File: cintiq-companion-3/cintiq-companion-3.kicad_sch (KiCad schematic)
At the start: 4 parts, among them J1 13HD_eDP, J2 13HD_penpanel, J3 13HD_buttonboard, J4 13HD_fingerpanel

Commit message: rotated images + ran some signals
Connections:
- net at J2.13 (Pin_13): now also J3.10 (Pin_10)
- net at J2.17 (Pin_17): now also J3.11 (Pin_11)
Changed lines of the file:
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@@
+	(wire
+		(pts
+			(xy 170.18 31.75) (xy 170.18 46.99)
+		)
+		(stroke
+			(width 0)
+			(type default)
+		)
+	)
 	(wire
 		(pts
@@
 	(wire
 		(pts
+			(xy 73.66 31.75) (xy 73.66 49.53)
+		)
+		(stroke
+			(width 0)
+			(type default)
+		)
+	)
+	(wire
+		(pts
 			(xy 157.48 33.02) (xy 151.13 33.02)
 		)
@@
 	(wire
 		(pts
+			(xy 170.18 46.99) (xy 83.82 46.99)
+		)
+		(stroke
+			(width 0)
+			(type default)
+		)
+	)
+	(wire
+		(pts
 			(xy 88.9 33.02) (xy 104.14 33.02)
 		)
@@
 	(wire
 		(pts
+			(xy 73.66 49.53) (xy 172.72 49.53)
+		)
+		(stroke
+			(width 0)
+			(type default)
+		)
+	)
+	(wire
+		(pts
 			(xy 248.92 64.77) (xy 248.92 109.22)
 		)
@@
 	(wire
 		(pts
+			(xy 83.82 46.99) (xy 83.82 31.75)
+		)
+		(stroke
+			(width 0)
+			(type default)
+		)
+	)
+	(wire
+		(pts
 			(xy 48.26 93.98) (xy 48.26 80.01)
 		)
 		(stroke
+			(width 0)
+			(type default)
+		)
+	)
+	(wire
+		(pts
+			(xy 172.72 31.75) (xy 172.72 49.53)
+		)
+		(stroke

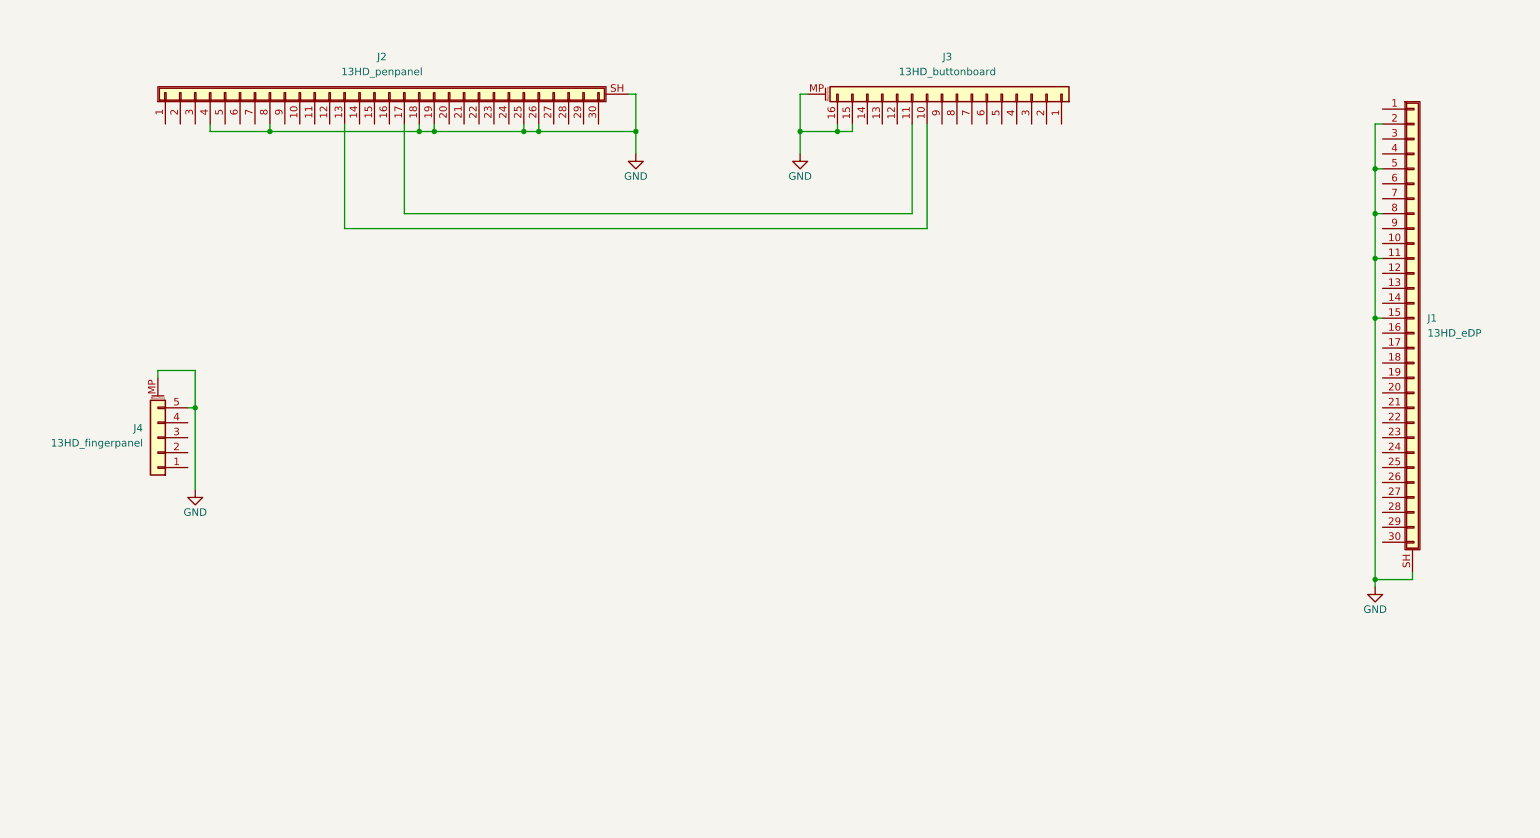
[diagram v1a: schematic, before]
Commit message: Added CP2102 usb uart bridge
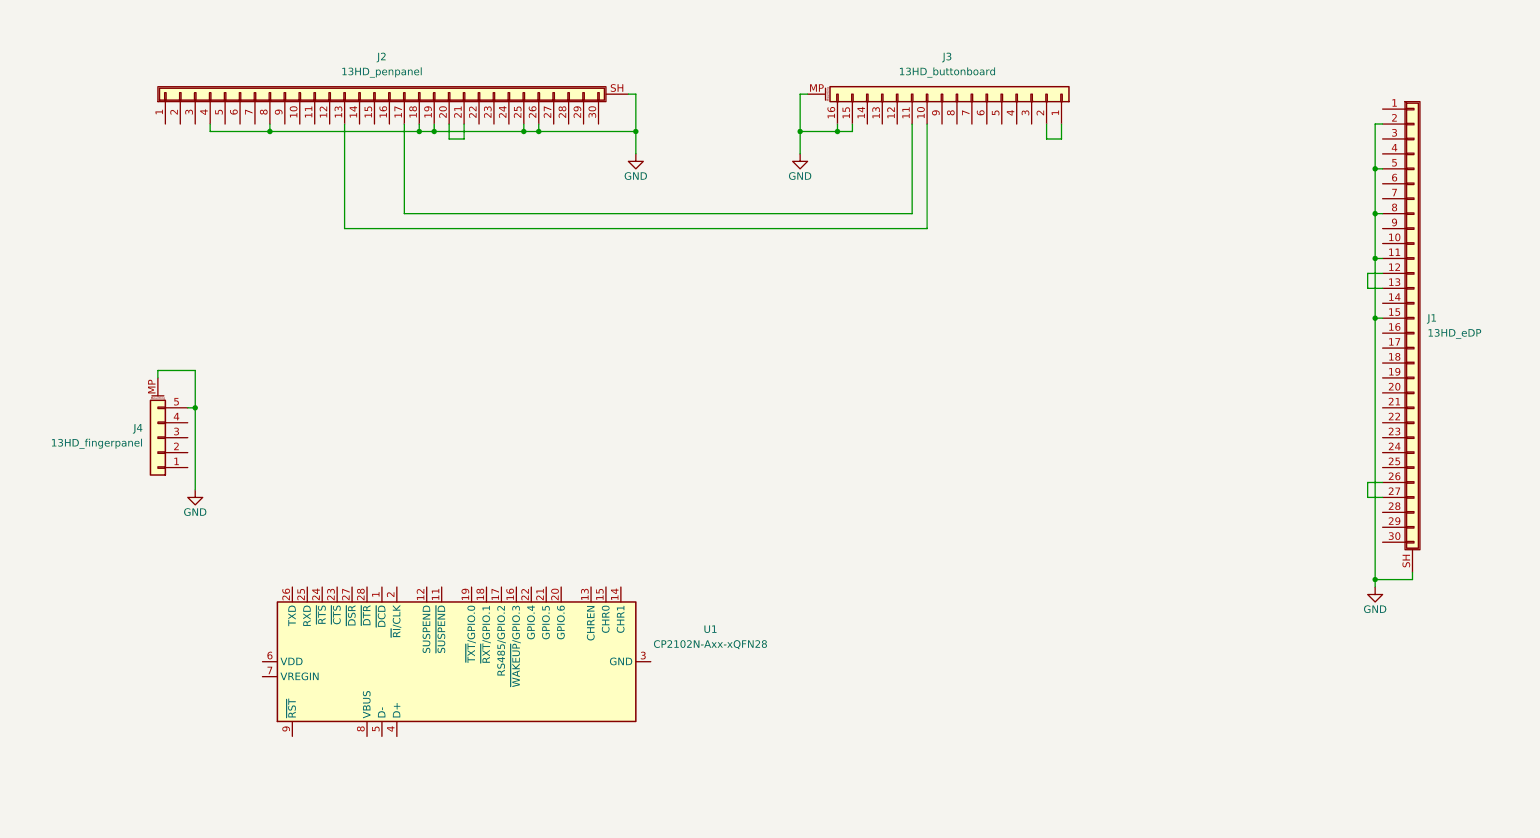
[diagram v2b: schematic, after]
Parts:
- added U1: CP2102N-Axx-xQFN28, Package_DFN_QFN:QFN-28-1EP_5x5mm_P0.5mm_EP3.35x3.35mm, symbol Interface_USB:CP2102N-Axx-xQFN28
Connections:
- net at J2.20 (Pin_20): now also J2.21 (Pin_21)
- net at J3.1 (Pin_1): now also J3.2 (Pin_2)
- net at J1.12 (Pin_12): now also J1.13 (Pin_13)
- net at J1.26 (Pin_26): now also J1.27 (Pin_27)
- new net: U1.29 (GND), U1.3 (GND)
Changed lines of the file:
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@@
+	(wire
+		(pts
+			(xy 195.58 34.29) (xy 193.04 34.29)
+		)
+		(stroke
+			(width 0)
+			(type default)
+		)
+	)
 	(wire
 		(pts
@@
 	(wire
 		(pts
+			(xy 250.19 57.15) (xy 247.65 57.15)
+		)
+		(stroke
+			(width 0)
+			(type default)
+		)
+	)
+	(wire
+		(pts
+			(xy 247.65 92.71) (xy 250.19 92.71)
+		)
+		(stroke
+			(width 0)
+			(type default)
+		)
+	)
+	(wire
+		(pts
 			(xy 170.18 31.75) (xy 170.18 46.99)
 		)
@@
 	(wire
 		(pts
+			(xy 250.19 95.25) (xy 247.65 95.25)
+		)
+		(stroke
+			(width 0)
+			(type default)
+		)
+	)
+	(wire
+		(pts
 			(xy 104.14 31.75) (xy 104.14 33.02)
 		)
@@
 	(wire
 		(pts
+			(xy 93.98 31.75) (xy 93.98 34.29)
+		)
+		(stroke
+			(width 0)
+			(type default)
+		)
+	)
+	(wire
+		(pts
+			(xy 247.65 59.69) (xy 250.19 59.69)
+		)
+		(stroke
+			(width 0)
+			(type default)
+		)
+	)
+	(wire
+		(pts
 			(xy 151.13 36.83) (xy 151.13 33.02)
 		)
@@
 	(wire
 		(pts
+			(xy 247.65 95.25) (xy 247.65 92.71)
+		)
+		(stroke
+			(width 0)
+			(type default)
+		)
+	)
+	(wire
+		(pts
 			(xy 106.68 33.02) (xy 123.19 33.02)
 		)
@@
 	(wire
 		(pts
+			(xy 91.44 34.29) (xy 91.44 31.75)
+		)
+		(stroke
+			(width 0)
+			(type default)
+		)
+	)
+	(wire
+		(pts
+			(xy 195.58 31.75) (xy 195.58 34.29)
+		)
+		(stroke
+			(width 0)
+			(type default)
+		)
+	)
+	(wire
+		(pts
 			(xy 248.92 64.77) (xy 248.92 109.22)
 		)
@@
 	(wire
 		(pts
+			(xy 193.04 34.29) (xy 193.04 31.75)
+		)
+		(stroke
+			(width 0)
+			(type default)
+		)
+	)
+	(wire
+		(pts
 			(xy 60.96 33.02) (xy 86.36 33.02)
 		)
@@
 	(wire
 		(pts
+			(xy 247.65 57.15) (xy 247.65 59.69)
+		)
+		(stroke
+			(width 0)
+			(type default)
+		)
+	)
+	(wire
+		(pts
 			(xy 123.19 33.02) (xy 123.19 26.67)
+		)
+		(stroke
+			(width 0)
+			(type default)
+		)
+	)
+	(wire
+		(pts
+			(xy 93.98 34.29) (xy 91.44 34.29)
 		)
 		(stroke
@@
 					(unit 1)
 				)
+			)
+		)
+	)
+	(symbol
+		(lib_id "Interface_USB:CP2102N-Axx-xQFN28")
+		(at 92.71 123.19 90)
+		(unit 1)
+		(exclude_from_sim no)
+		(in_bom yes)
+		(on_board yes)
+		(dnp no)
+		(fields_autoplaced yes)
+		(property "Reference" "U1"
+			(at 135.89 117.6938 90)
+			(effects
+				(font
+					(size 1.27 1.27)
+				)
+			)
+		)
+		(property "Value" "CP2102N-Axx-xQFN28"
+			(at 135.89 120.2338 90)
+			(effects
+				(font
+					(size 1.27 1.27)
+				)
+			)
+		)
+		(property "Footprint" "Package_DFN_QFN:QFN-28-1EP_5x5mm_P0.5mm_EP3.35x3.35mm"
+			(at 124.46 90.17 0)
+			(effects
+				(font
+					(size 1.27 1.27)
+				)
+				(hide yes)
+			)
+		)
+		(property "Datasheet" "https://www.silabs.com/documents/public/data-sheets/cp2102n-datasheet.pdf"
+			(at 111.76 121.92 0)
+			(effects
+				(font
+					(size 1.27 1.27)
+				)
+				(hide yes)
+			)
+		)
+		(property "Description" "USB to UART master bridge, QFN-28"
+			(at 92.71 123.19 0)
+			(effects
+				(font
+					(size 1.27 1.27)
+				)
+				(hide yes)
+			)
+		)
+		(pin "13"
+		)
+		(pin "5"
+		)
+		(pin "29"
+		)
+		(pin "2"
+		)
+		(pin "9"
+		)
+		(pin "23"
+		)
+		(pin "24"
+		)
+		(pin "25"
+		)
+		(pin "15"
+		)
+		(pin "26"
+		)
+		(pin "3"
+		)
+		(pin "7"
+		)
+		(pin "8"
+		)
+		(pin "14"
+		)
+		(pin "1"
+		)
+		(pin "18"
+		)
+		(pin "19"
+		)
+		(pin "17"
+		)
+		(pin "21"
+		)
+		(pin "22"
+		)
+		(pin "27"
+		)
+		(pin "11"
+		)
+		(pin "12"
+		)
+		(pin "10"
+		)
+		(pin "16"
+		)
+		(pin "20"
+		)
+		(pin "28"
+		)
+		(pin "4"
+		)
+		(pin "6"
+		)
+		(instances
+			(project "cintiq-companion-3"
+				(path "/ef92970f-f7a1-4011-9c13-6d46a45b923d"
+					(reference "U1")
+					(unit 1)
+				)

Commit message: Added USB pins for touch and pen panels
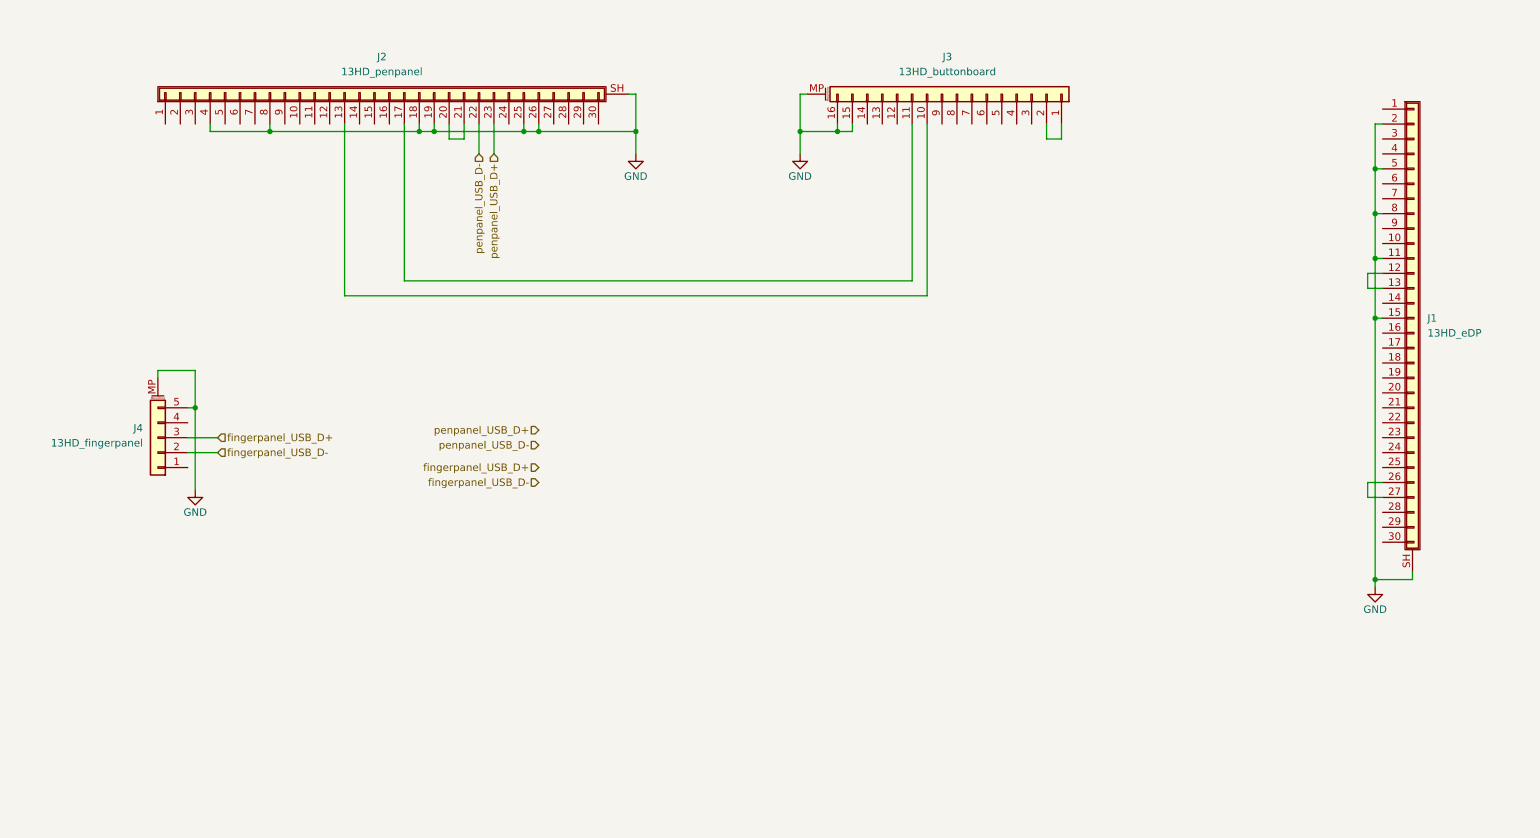
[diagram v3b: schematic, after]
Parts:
- removed U1: CP2102N-Axx-xQFN28, Package_DFN_QFN:QFN-28-1EP_5x5mm_P0.5mm_EP3.35x3.35mm, symbol Interface_USB:CP2102N-Axx-xQFN28
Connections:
- net penpanel_USB_D-: now reaches J2.22 (Pin_22)
- net penpanel_USB_D+: now reaches J2.23 (Pin_23)
- net fingerpanel_USB_D-: now reaches J4.2 (Pin_2)
- net fingerpanel_USB_D+: now reaches J4.3 (Pin_3)
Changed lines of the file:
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@@
 	(wire
 		(pts
-			(xy 170.18 31.75) (xy 170.18 46.99)
+			(xy 170.18 31.75) (xy 170.18 58.42)
 		)
 		(stroke
@@
 	(wire
 		(pts
+			(xy 52.07 85.09) (xy 46.99 85.09)
+		)
+		(stroke
+			(width 0)
+			(type default)
+		)
+	)
+	(wire
+		(pts
 			(xy 250.19 31.75) (xy 248.92 31.75)
 		)
@@
 	(wire
 		(pts
-			(xy 73.66 31.75) (xy 73.66 49.53)
+			(xy 73.66 31.75) (xy 73.66 60.96)
 		)
 		(stroke
@@
 	(wire
 		(pts
-			(xy 170.18 46.99) (xy 83.82 46.99)
+			(xy 170.18 58.42) (xy 83.82 58.42)
 		)
 		(stroke
@@
 	(wire
 		(pts
-			(xy 73.66 49.53) (xy 172.72 49.53)
+			(xy 73.66 60.96) (xy 172.72 60.96)
 		)
 		(stroke
@@
 	(wire
 		(pts
-			(xy 83.82 46.99) (xy 83.82 31.75)
+			(xy 83.82 58.42) (xy 83.82 31.75)
 		)
 		(stroke
@@
 	(wire
 		(pts
-			(xy 172.72 31.75) (xy 172.72 49.53)
+			(xy 172.72 31.75) (xy 172.72 60.96)
 		)
 		(stroke
@@
 	(wire
 		(pts
+			(xy 99.06 36.83) (xy 99.06 31.75)
+		)
+		(stroke
+			(width 0)
+			(type default)
+		)
+	)
+	(wire
+		(pts
 			(xy 160.02 33.02) (xy 157.48 33.02)
 		)
@@
 	(wire
 		(pts
+			(xy 52.07 87.63) (xy 46.99 87.63)
+		)
+		(stroke
+			(width 0)
+			(type default)
+		)
+	)
+	(wire
+		(pts
 			(xy 248.92 110.49) (xy 248.92 109.22)
 		)
@@
 	(wire
 		(pts
+			(xy 96.52 31.75) (xy 96.52 36.83)
+		)
+		(stroke
+			(width 0)
+			(type default)
+		)
+	)
+	(wire
+		(pts
 			(xy 60.96 33.02) (xy 86.36 33.02)
 		)
@@
 			(width 0)
 			(type default)
+		)
+	)
+	(hierarchical_label "penpanel_USB_D-"
+		(shape input)
+		(at 106.68 86.36 180)
+		(fields_autoplaced yes)
+		(effects
+			(font
+				(size 1.27 1.27)
+			)
+			(justify right)
+		)
+	)
+	(hierarchical_label "fingerpanel_USB_D-"
+		(shape input)
+		(at 52.07 87.63 0)
+		(fields_autoplaced yes)
+		(effects
+			(font
+				(size 1.27 1.27)
+			)
+			(justify left)
+		)
+	)
+	(hierarchical_label "fingerpanel_USB_D-"
+		(shape input)
+		(at 106.68 92.71 180)
+		(fields_autoplaced yes)
+		(effects
+			(font
+				(size 1.27 1.27)
+			)
+			(justify right)
+		)
+	)
+	(hierarchical_label "fingerpanel_USB_D+"
+		(shape input)
+		(at 106.68 90.17 180)
+		(fields_autoplaced yes)
+		(effects
+			(font
+				(size 1.27 1.27)
+			)
+			(justify right)
+		)
+	)
+	(hierarchical_label "penpanel_USB_D-"
+		(shape input)
+		(at 96.52 36.83 270)
+		(fields_autoplaced yes)
+		(effects
+			(font
+				(size 1.27 1.27)
+			)
+			(justify right)
+		)
+	)
+	(hierarchical_label "penpanel_USB_D+"
+		(shape input)
+		(at 106.68 83.82 180)
+		(fields_autoplaced yes)
+		(effects
+			(font
+				(size 1.27 1.27)
+			)
+			(justify right)
+		)
+	)
+	(hierarchical_label "fingerpanel_USB_D+"
+		(shape input)
+		(at 52.07 85.09 0)
+		(fields_autoplaced yes)
+		(effects
+			(font
+				(size 1.27 1.27)
+			)
+			(justify left)
+		)
+	)
+	(hierarchical_label "penpanel_USB_D+"
+		(shape input)
+		(at 99.06 36.83 270)
+		(fields_autoplaced yes)
+		(effects
+			(font
+				(size 1.27 1.27)
+			)
+			(justify right)
 		)
 	)
@@
 					(unit 1)
 				)
-			)
-		)
-	)
-	(symbol
-		(lib_id "Interface_USB:CP2102N-Axx-xQFN28")
-		(at 92.71 123.19 90)
-		(unit 1)
-		(exclude_from_sim no)
-		(in_bom yes)
-		(on_board yes)
-		(dnp no)
-		(fields_autoplaced yes)
-		(property "Reference" "U1"
-			(at 135.89 117.6938 90)
-			(effects
-				(font
-					(size 1.27 1.27)
-				)
-			)
-		)
-		(property "Value" "CP2102N-Axx-xQFN28"
-			(at 135.89 120.2338 90)
-			(effects
-				(font
-					(size 1.27 1.27)
-				)
-			)
-		)
-		(property "Footprint" "Package_DFN_QFN:QFN-28-1EP_5x5mm_P0.5mm_EP3.35x3.35mm"
-			(at 124.46 90.17 0)
-			(effects
-				(font
-					(size 1.27 1.27)
-				)
-				(hide yes)
-			)
-		)
-		(property "Datasheet" "https://www.silabs.com/documents/public/data-sheets/cp2102n-datasheet.pdf"
-			(at 111.76 121.92 0)
-			(effects
-				(font
-					(size 1.27 1.27)
-				)
-				(hide yes)
-			)
-		)
-		(property "Description" "USB to UART master bridge, QFN-28"
-			(at 92.71 123.19 0)
-			(effects
-				(font
-					(size 1.27 1.27)
-				)
-				(hide yes)
-			)
-		)
-		(pin "13"
-		)
-		(pin "5"
-		)
-		(pin "29"
-		)
-		(pin "2"
-		)
-		(pin "9"
-		)
-		(pin "23"
-		)
-		(pin "24"
-		)
-		(pin "25"
-		)
-		(pin "15"
-		)
-		(pin "26"
-		)
-		(pin "3"
-		)
-		(pin "7"
-		)
-		(pin "8"
-		)
-		(pin "14"
-		)
-		(pin "1"
-		)
-		(pin "18"
-		)
-		(pin "19"
-		)
-		(pin "17"
-		)
-		(pin "21"
-		)
-		(pin "22"
-		)
-		(pin "27"
-		)
-		(pin "11"
-		)
-		(pin "12"
-		)
-		(pin "10"
-		)
-		(pin "16"
-		)
-		(pin "20"
-		)
-		(pin "28"
-		)
-		(pin "4"
-		)
-		(pin "6"
-		)
-		(instances
-			(project "cintiq-companion-3"
-				(path "/ef92970f-f7a1-4011-9c13-6d46a45b923d"
-					(reference "U1")
-					(unit 1)
-				)

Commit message: Added power rails
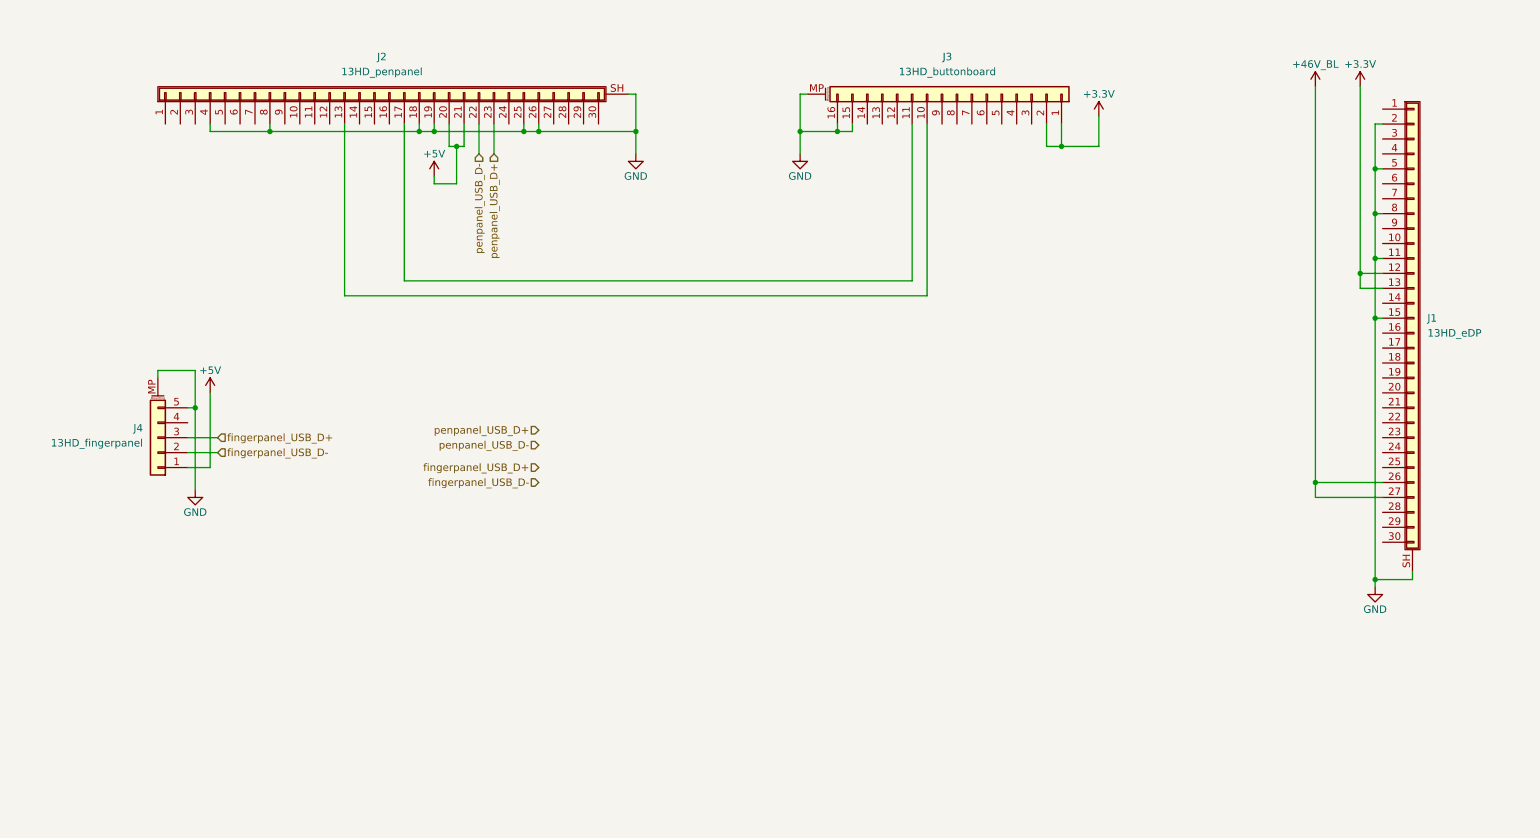
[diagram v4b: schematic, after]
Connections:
- net +5V: now reaches J2.20 (Pin_20), J2.21 (Pin_21)
- net +5V: now also J4.1 (Pin_1)
- net +3.3V: now reaches J3.1 (Pin_1), J3.2 (Pin_2)
- net +3.3V: now also J1.12 (Pin_12), J1.13 (Pin_13)
- net +46V_BL: now reaches J1.26 (Pin_26), J1.27 (Pin_27)
